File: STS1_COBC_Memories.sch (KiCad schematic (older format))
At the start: 2 parts

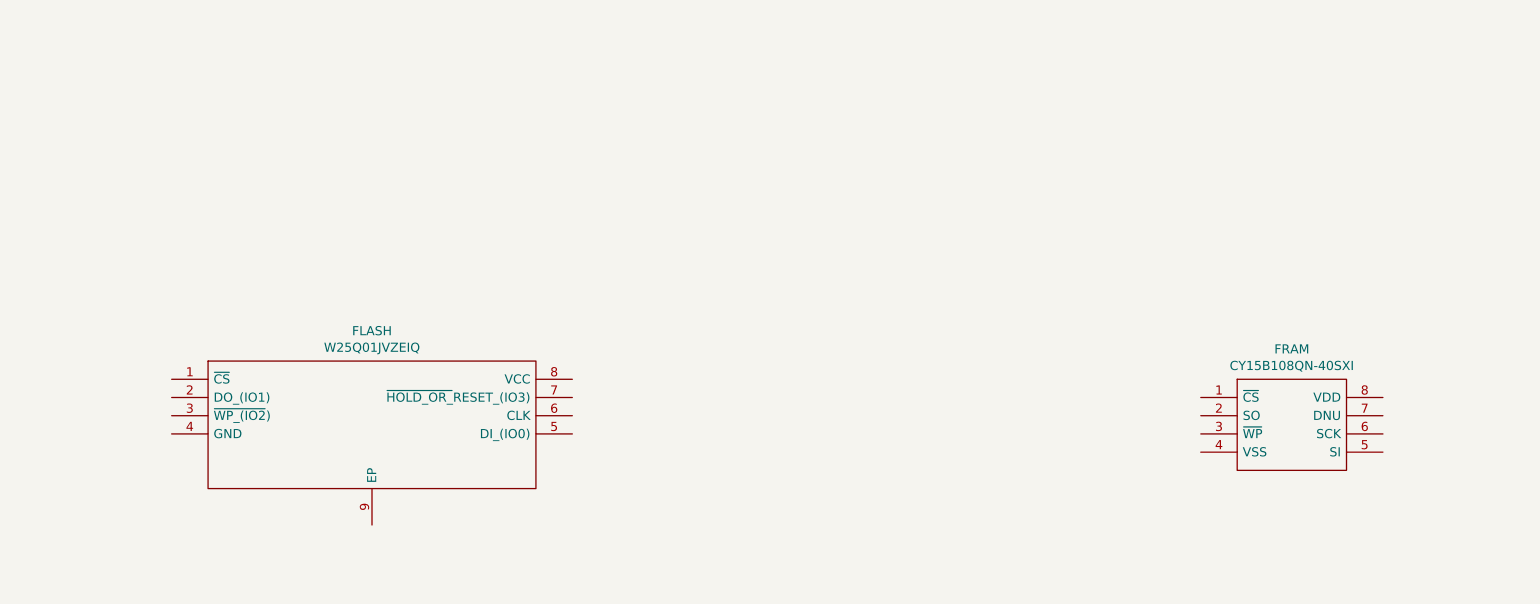
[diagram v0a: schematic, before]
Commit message: RF modules added + some tweaking on STM32
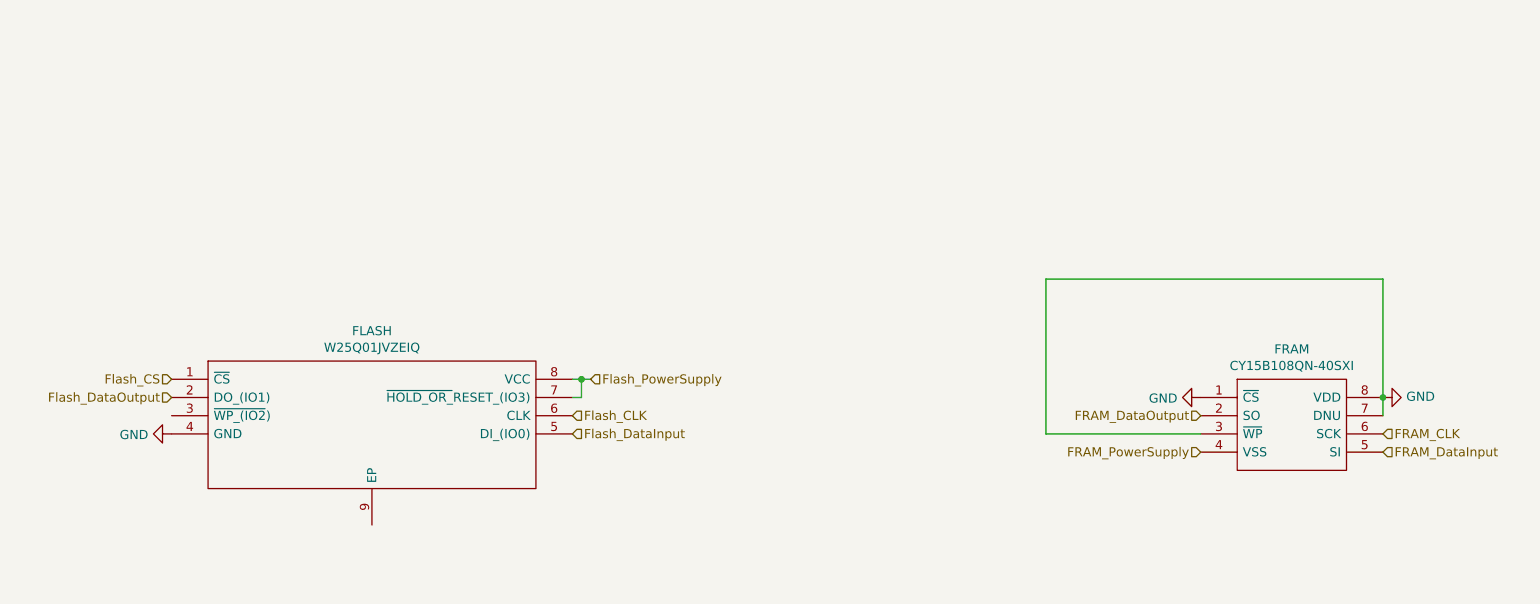
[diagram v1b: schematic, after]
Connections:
- net Flash_CS: now reaches FLASH.1 (~CS)
- net Flash_DataOutput: now reaches FLASH.2 (DO_(IO1))
- net GND: now reaches FLASH.4 (GND)
- net GND: now also FRAM.1 (~CS), FRAM.3 (~WP), FRAM.7 (DNU), FRAM.8 (VDD)
- net Flash_DataInput: now reaches FLASH.5 (DI_(IO0))
- net Flash_CLK: now reaches FLASH.6 (CLK)
- net Flash_PowerSupply: now reaches FLASH.7 (~HOLD_OR_~RESET_(IO3))
- net Flash_PowerSupply: now also FLASH.8 (VCC)
- net FRAM_DataOutput: now reaches FRAM.2 (SO)
- net FRAM_PowerSupply: now reaches FRAM.4 (VSS)
- net FRAM_DataInput: now reaches FRAM.5 (SI)
- net FRAM_CLK: now reaches FRAM.6 (SCK)
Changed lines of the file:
@@
 $Descr A4 11693 8268
 encoding utf-8
-Sheet 4 4
+Sheet 4 7
 Title ""
 Date ""
@@
 	1    0    0    -1
 $EndComp
+Text HLabel 4300 3000 2    50   Input ~ 0
+Flash_CLK
+Text HLabel 4400 2800 2    50   Input ~ 0
+Flash_PowerSupply
+Text HLabel 4300 3100 2    50   Input ~ 0
+Flash_DataInput
+Text HLabel 2100 2900 0    50   Input ~ 0
+Flash_DataOutput
+Text HLabel 2100 2800 0    50   Input ~ 0
+Flash_CS
+Text HLabel 8750 3100 2    50   Input ~ 0
+FRAM_CLK
+Text HLabel 8750 3200 2    50   Input ~ 0
+FRAM_DataInput
+Text HLabel 7750 3000 0    50   Input ~ 0
+FRAM_DataOutput
+Text HLabel 7750 3200 0    50   Input ~ 0
+FRAM_PowerSupply
+$Comp
+L power:GND #PWR?
+U 1 1 61291A0F
+P 2100 3100
+F 0 "#PWR?" H 2100 2850 50  0001 C CNN
+F 1 "GND" V 2105 2972 50  0000 R CNN
+F 2 "" H 2100 3100 50  0001 C CNN
+F 3 "" H 2100 3100 50  0001 C CNN
+	1    2100 3100
+	0    1    1    0
+$EndComp
+$Comp
+L power:GND #PWR?
+U 1 1 6129295C
+P 8750 2900
+F 0 "#PWR?" H 8750 2650 50  0001 C CNN
+F 1 "GND" V 8755 2772 50  0000 R CNN
+F 2 "" H 8750 2900 50  0001 C CNN
+F 3 "" H 8750 2900 50  0001 C CNN
+	1    8750 2900
+	0    -1   -1   0
+$EndComp
+Wire Wire Line
+	8750 3000 8750 2900
+Connection ~ 8750 2900
+Wire Wire Line
+	6900 3100 6900 2250
+Wire Wire Line
+	6900 2250 8750 2250
+Wire Wire Line
+	8750 2250 8750 2900
+Wire Wire Line
+	6900 3100 7750 3100
+$Comp
+L power:GND #PWR?
+U 1 1 612BEAFE
+P 7750 2900
+F 0 "#PWR?" H 7750 2650 50  0001 C CNN
+F 1 "GND" V 7755 2772 50  0000 R CNN
+F 2 "" H 7750 2900 50  0001 C CNN
+F 3 "" H 7750 2900 50  0001 C CNN
+	1    7750 2900
+	0    1    1    0
+$EndComp
+Wire Wire Line
+	4300 2800 4350 2800
+Wire Wire Line
+	4350 2800 4350 2900
+Wire Wire Line
+	4350 2900 4300 2900
+Connection ~ 4350 2800
+Wire Wire Line
+	4350 2800 4400 2800
 $EndSCHEMATC

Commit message: finished schematic
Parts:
- FLASH1: renamed from FLASH; footprint SON127P800X600X80-9N-D -> W25Q01JVZEIQ:SON127P800X600X80-9N-D
- FRAM1: renamed from FRAM; footprint SOIC127P800X203-8N -> CY15B108QN-40SXI:SOIC127P800X203-8N
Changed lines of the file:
@@
 $EndDescr
 $Comp
-L W25Q01JVZEIQ:W25Q01JVZEIQ FLASH
+L W25Q01JVZEIQ:W25Q01JVZEIQ FLASH1
 U 1 1 612A5631
 P 2100 2800
-F 0 "FLASH" H 3200 3065 50  0000 C CNN
+F 0 "FLASH1" H 3200 3065 50  0000 C CNN
 F 1 "W25Q01JVZEIQ" H 3200 2974 50  0000 C CNN
-F 2 "SON127P800X600X80-9N-D" H 4150 2900 50  0001 L CNN
+F 2 "W25Q01JVZEIQ:SON127P800X600X80-9N-D" H 4150 2900 50  0001 L CNN
 F 3 "https://4donline.ihs.com/images/VipMasterIC/IC/WBND/WBND-S-A0009189314/WBND-S-A0009189314-1.pdf?hkey=EF798316E3902B6ED9A73243A3159BB0" H 4150 2800 50  0001 L CNN
 F 4 "NOR Flash spiFlash, 1G-bit, 4Kb Uniform Sector" H 4150 2700 50  0001 L CNN "Description"
@@
 $EndComp
 $Comp
-L CY15B108QN-40SXI:CY15B108QN-40SXI FRAM
+L CY15B108QN-40SXI:CY15B108QN-40SXI FRAM1
 U 1 1 612A5F08
 P 7750 2900
-F 0 "FRAM" H 8250 3165 50  0000 C CNN
+F 0 "FRAM1" H 8250 3165 50  0000 C CNN
 F 1 "CY15B108QN-40SXI" H 8250 3074 50  0000 C CNN
-F 2 "SOIC127P800X203-8N" H 8600 3000 50  0001 L CNN
+F 2 "CY15B108QN-40SXI:SOIC127P800X203-8N" H 8600 3000 50  0001 L CNN
 F 3 "https://www.cypress.com/file/444186/download" H 8600 2900 50  0001 L CNN
 F 4 "CY15B108QN-40SXI" H 8600 2800 50  0001 L CNN "Description"
@@
 FRAM_PowerSupply
 $Comp
-L power:GND #PWR?
+L power:GND #PWR0139
 U 1 1 61291A0F
 P 2100 3100
-F 0 "#PWR?" H 2100 2850 50  0001 C CNN
+F 0 "#PWR0139" H 2100 2850 50  0001 C CNN
 F 1 "GND" V 2105 2972 50  0000 R CNN
 F 2 "" H 2100 3100 50  0001 C CNN
@@
 $EndComp
 $Comp
-L power:GND #PWR?
+L power:GND #PWR0140
 U 1 1 6129295C
 P 8750 2900
-F 0 "#PWR?" H 8750 2650 50  0001 C CNN
+F 0 "#PWR0140" H 8750 2650 50  0001 C CNN
 F 1 "GND" V 8755 2772 50  0000 R CNN
 F 2 "" H 8750 2900 50  0001 C CNN
@@
 	6900 3100 7750 3100
 $Comp
-L power:GND #PWR?
+L power:GND #PWR0141
 U 1 1 612BEAFE
 P 7750 2900
-F 0 "#PWR?" H 7750 2650 50  0001 C CNN
+F 0 "#PWR0141" H 7750 2650 50  0001 C CNN
 F 1 "GND" V 7755 2772 50  0000 R CNN
 F 2 "" H 7750 2900 50  0001 C CNN

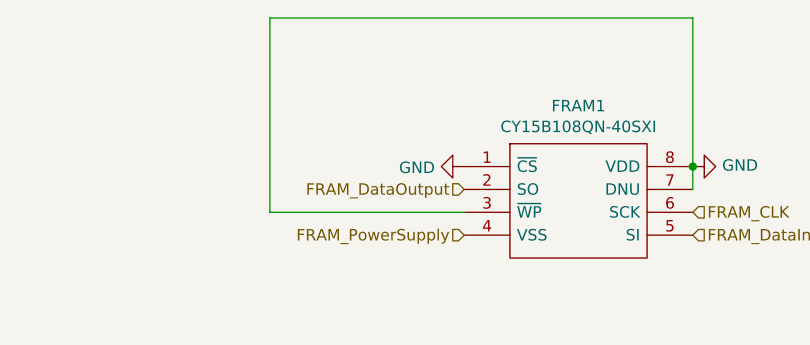
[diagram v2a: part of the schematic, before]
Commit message: BuckBoost added
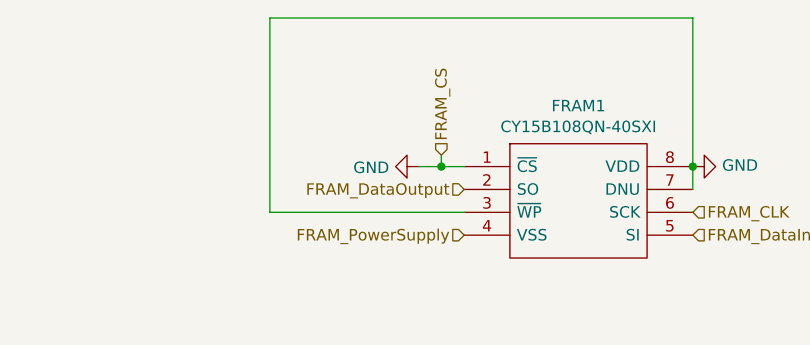
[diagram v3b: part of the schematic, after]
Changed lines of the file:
@@
 L power:GND #PWR0141
 U 1 1 612BEAFE
-P 7750 2900
-F 0 "#PWR0141" H 7750 2650 50  0001 C CNN
-F 1 "GND" V 7755 2772 50  0000 R CNN
-F 2 "" H 7750 2900 50  0001 C CNN
-F 3 "" H 7750 2900 50  0001 C CNN
-	1    7750 2900
+P 7550 2900
+F 0 "#PWR0141" H 7550 2650 50  0001 C CNN
+F 1 "GND" V 7555 2772 50  0000 R CNN
+F 2 "" H 7550 2900 50  0001 C CNN
+F 3 "" H 7550 2900 50  0001 C CNN
+	1    7550 2900
 	0    1    1    0
 $EndComp
@@
 Wire Wire Line
 	4350 2800 4400 2800
+Text HLabel 7650 2850 1    50   Input ~ 0
+FRAM_CS
+Wire Wire Line
+	7750 2900 7650 2900
+Wire Wire Line
+	7650 2850 7650 2900
+Connection ~ 7650 2900
+Wire Wire Line
+	7650 2900 7550 2900
 $EndSCHEMATC

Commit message: schematic done
final tweaks (adding LEDS, pin headers, moving circuits...)
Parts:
- added C? (x2): 100n, symbol Device:C
- added C? (x2): 47u, symbol Device:C
- added JP2: Jumper_NC_Dual, symbol Device:Jumper_NC_Dual
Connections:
- net FRAM_PowerSupply: now also FRAM1.8 (VDD), C?.2, C?.2; no longer FRAM1.4 (VSS)
- net Flash_PowerSupply: now also C?.2, C?.2, JP2.1; no longer FLASH1.7 (~HOLD_OR_~RESET_(IO3))
- net GND: now also FRAM1.4 (VSS), C?.1, C?.1, C?.1, C?.1, JP2.3; no longer FRAM1.1 (~CS), FRAM1.3 (~WP), FRAM1.8 (VDD)
- net Flash_WP: now reaches FLASH1.3 (~WP_(IO2))
- new net: FLASH1.7 (~HOLD_OR_~RESET_(IO3)), JP2.2
- new net FRAM_CS: FRAM1.1 (~CS)
- new net FRAM_WP: FRAM1.3 (~WP)
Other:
- note added: "EP pin ??\n"
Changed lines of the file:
@@
 $Descr A4 11693 8268
 encoding utf-8
-Sheet 4 7
+Sheet 2 5
 Title ""
 Date ""
@@
 Text HLabel 4300 3000 2    50   Input ~ 0
 Flash_CLK
-Text HLabel 4400 2800 2    50   Input ~ 0
+Text HLabel 4400 1700 1    50   Input ~ 0
 Flash_PowerSupply
 Text HLabel 4300 3100 2    50   Input ~ 0
@@
 Text HLabel 7750 3000 0    50   Input ~ 0
 FRAM_DataOutput
-Text HLabel 7750 3200 0    50   Input ~ 0
+Text HLabel 8750 1700 1    50   Input ~ 0
 FRAM_PowerSupply
 $Comp
@@
 L power:GND #PWR0140
 U 1 1 6129295C
-P 8750 2900
-F 0 "#PWR0140" H 8750 2650 50  0001 C CNN
-F 1 "GND" V 8755 2772 50  0000 R CNN
-F 2 "" H 8750 2900 50  0001 C CNN
-F 3 "" H 8750 2900 50  0001 C CNN
-	1    8750 2900
-	0    -1   -1   0
-$EndComp
-Wire Wire Line
-	8750 3000 8750 2900
-Connection ~ 8750 2900
-Wire Wire Line
-	6900 3100 6900 2250
-Wire Wire Line
-	6900 2250 8750 2250
-Wire Wire Line
-	8750 2250 8750 2900
+P 7750 3200
+F 0 "#PWR0140" H 7750 2950 50  0001 C CNN
+F 1 "GND" V 7755 3072 50  0000 R CNN
+F 2 "" H 7750 3200 50  0001 C CNN
+F 3 "" H 7750 3200 50  0001 C CNN
+	1    7750 3200
+	0    1    1    0
+$EndComp
 Wire Wire Line
 	6900 3100 7750 3100
-$Comp
-L power:GND #PWR0141
-U 1 1 612BEAFE
-P 7550 2900
-F 0 "#PWR0141" H 7550 2650 50  0001 C CNN
-F 1 "GND" V 7555 2772 50  0000 R CNN
-F 2 "" H 7550 2900 50  0001 C CNN
-F 3 "" H 7550 2900 50  0001 C CNN
-	1    7550 2900
-	0    1    1    0
-$EndComp
-Wire Wire Line
-	4300 2800 4350 2800
-Wire Wire Line
-	4350 2800 4350 2900
-Wire Wire Line
-	4350 2900 4300 2900
-Connection ~ 4350 2800
-Wire Wire Line
-	4350 2800 4400 2800
 Text HLabel 7650 2850 1    50   Input ~ 0
 FRAM_CS
@@
 Wire Wire Line
 	7650 2850 7650 2900
-Connection ~ 7650 2900
-Wire Wire Line
-	7650 2900 7550 2900
+Text HLabel 2100 3000 0    50   Input ~ 0
+Flash_WP
+Text Notes 3100 3750 0    50   ~ 0
+EP pin ??\n
+Wire Wire Line
+	4300 2800 4400 2800
+$Comp
+L Device:Jumper_NC_Dual JP2
+U 1 1 616C1C39
+P 5050 2800
+F 0 "JP2" V 5004 2902 50  0000 L CNN
+F 1 "Jumper_NC_Dual" V 5095 2902 50  0000 L CNN
+F 2 "" H 5050 2800 50  0001 C CNN
+F 3 "~" H 5050 2800 50  0001 C CNN
+	1    5050 2800
+	0    1    1    0
+$EndComp
+$Comp
+L power:GND #PWR0123
+U 1 1 616C2B2C
+P 5050 3050
+F 0 "#PWR0123" H 5050 2800 50  0001 C CNN
+F 1 "GND" V 5055 2922 50  0000 R CNN
+F 2 "" H 5050 3050 50  0001 C CNN
+F 3 "" H 5050 3050 50  0001 C CNN
+	1    5050 3050
+	1    0    0    -1
+$EndComp
+Wire Wire Line
+	4850 2900 4850 2800
+Wire Wire Line
+	4850 2800 4950 2800
+Wire Wire Line
+	4300 2900 4850 2900
+Wire Wire Line
+	5050 2550 4700 2550
+Wire Wire Line
+	4700 2550 4700 2800
+Wire Wire Line
+	4700 2800 4400 2800
+Connection ~ 4400 2800
+Text HLabel 6900 3100 0    50   Input ~ 0
+FRAM_WP
+$Comp
+L power:GND #PWR0141
+U 1 1 616C77F0
+P 8750 3000
+F 0 "#PWR0141" H 8750 2750 50  0001 C CNN
+F 1 "GND" V 8755 2872 50  0000 R CNN
+F 2 "" H 8750 3000 50  0001 C CNN
+F 3 "" H 8750 3000 50  0001 C CNN
+	1    8750 3000
+	0    -1   -1   0
+$EndComp
+$Comp
+L Device:C C?
+U 1 1 61691DC4
+P 4650 1850
+F 0 "C?" V 4398 1850 50  0000 C CNN
+F 1 "100n" V 4489 1850 50  0000 C CNN
+F 2 "" H 4688 1700 50  0001 C CNN
+F 3 "~" H 4650 1850 50  0001 C CNN
+	1    4650 1850
+	0    1    1    0
+$EndComp
+$Comp
+L Device:C C?
+U 1 1 61692327
+P 4650 2200
+F 0 "C?" V 4398 2200 50  0000 C CNN
+F 1 "47u" V 4489 2200 50  0000 C CNN
+F 2 "" H 4688 2050 50  0001 C CNN
+F 3 "~" H 4650 2200 50  0001 C CNN
+	1    4650 2200
+	0    1    1    0
+$EndComp
+$Comp
+L power:GND #PWR?
+U 1 1 61692683
+P 4800 2200
+F 0 "#PWR?" H 4800 1950 50  0001 C CNN
+F 1 "GND" V 4805 2072 50  0000 R CNN
+F 2 "" H 4800 2200 50  0001 C CNN
+F 3 "" H 4800 2200 50  0001 C CNN
+	1    4800 2200
+	0    -1   -1   0
+$EndComp
+$Comp
+L power:GND #PWR?
+U 1 1 61692ABE
+P 4800 1850
+F 0 "#PWR?" H 4800 1600 50  0001 C CNN
+F 1 "GND" V 4805 1722 50  0000 R CNN
+F 2 "" H 4800 1850 50  0001 C CNN
+F 3 "" H 4800 1850 50  0001 C CNN
+	1    4800 1850
+	0    -1   -1   0
+$EndComp
+Wire Wire Line
+	4400 1700 4400 1850
+Wire Wire Line
+	4400 2200 4500 2200
+Connection ~ 4400 2200
+Wire Wire Line
+	4400 2200 4400 2800
+Wire Wire Line
+	4400 1850 4500 1850
+Connection ~ 4400 1850
+Wire Wire Line
+	4400 1850 4400 2200
+$Comp
+L Device:C C?
+U 1 1 61694B9B
+P 8900 1900
+F 0 "C?" V 8648 1900 50  0000 C CNN
+F 1 "100n" V 8739 1900 50  0000 C CNN
+F 2 "" H 8938 1750 50  0001 C CNN
+F 3 "~" H 8900 1900 50  0001 C CNN
+	1    8900 1900
+	0    1    1    0
+$EndComp
+$Comp
+L Device:C C?
+U 1 1 61694BA1
+P 8900 2250
+F 0 "C?" V 8648 2250 50  0000 C CNN
+F 1 "47u" V 8739 2250 50  0000 C CNN
+F 2 "" H 8938 2100 50  0001 C CNN
+F 3 "~" H 8900 2250 50  0001 C CNN
+	1    8900 2250
+	0    1    1    0
+$EndComp
+$Comp
+L power:GND #PWR?
+U 1 1 61694BA7
+P 9050 2250
+F 0 "#PWR?" H 9050 2000 50  0001 C CNN
+F 1 "GND" V 9055 2122 50  0000 R CNN
+F 2 "" H 9050 2250 50  0001 C CNN
+F 3 "" H 9050 2250 50  0001 C CNN
+	1    9050 2250
+	0    -1   -1   0
+$EndComp
+$Comp
+L power:GND #PWR?
+U 1 1 61694BAD
+P 9050 1900
+F 0 "#PWR?" H 9050 1650 50  0001 C CNN
+F 1 "GND" V 9055 1772 50  0000 R CNN
+F 2 "" H 9050 1900 50  0001 C CNN
+F 3 "" H 9050 1900 50  0001 C CNN
+	1    9050 1900
+	0    -1   -1   0
+$EndComp
+Wire Wire Line
+	8750 1700 8750 1900
+Connection ~ 8750 1900
+Wire Wire Line
+	8750 1900 8750 2250
+Connection ~ 8750 2250
+Wire Wire Line
+	8750 2250 8750 2900
 $EndSCHEMATC
